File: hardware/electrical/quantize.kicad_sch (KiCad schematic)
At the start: 5 parts

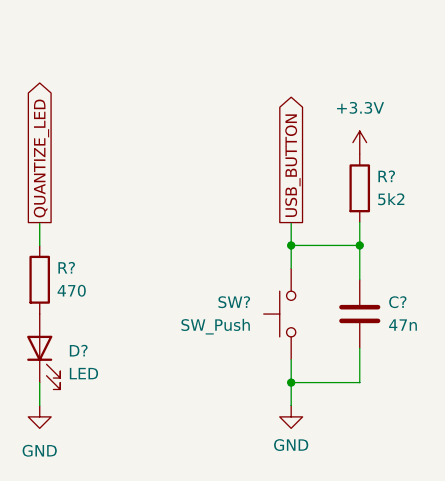
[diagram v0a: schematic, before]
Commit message: Schematic rev. 2 Add second microcontroller to handle encoder, buttons and LEDs Remove external pull-up resistors Simplify LED driver circuits Remove debouncing capacitors Rename SPI connections with standard names Use SPI1 rather than SPI2 Isolate GNDD and GLED
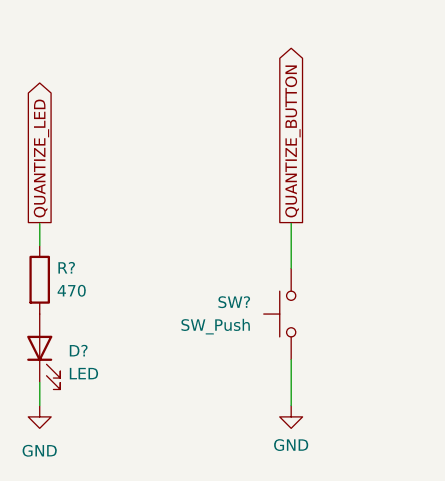
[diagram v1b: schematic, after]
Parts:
- removed C?: 47n, symbol Device:C
- removed R?: 5k2, symbol Device:R
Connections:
- net USB_BUTTON renamed QUANTIZE_BUTTON
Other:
- company: (none) -> © ANDREI ANATSKA, FRANK PLOWMAN 2022
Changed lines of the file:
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@@
 (kicad_sch (version 20211123) (generator eeschema)
   (paper "A4")
-  (junction (at 157.48 113.665) (diameter 0) (color 0 0 0 0)
+  (title_block
+    (date "2022-09-08")
+    (rev "2")
+    (company "© ANDREI ANATSKA, FRANK PLOWMAN 2022")
   )
-  (junction (at 165.1 98.425) (diameter 0) (color 0 0 0 0)
-  )
-  (junction (at 157.48 98.425) (diameter 0) (color 0 0 0 0)
-  )
-  (wire (pts (xy 165.1 102.235) (xy 165.1 98.425))
-    (stroke (width 0) (type default) (color 0 0 0 0))
-  )
-  (wire (pts (xy 157.48 113.665) (xy 165.1 113.665))
-    (stroke (width 0) (type default) (color 0 0 0 0))
-  )
-  (wire (pts (xy 157.48 98.425) (xy 165.1 98.425))
-    (stroke (width 0) (type default) (color 0 0 0 0))
-  )
-  (wire (pts (xy 165.1 113.665) (xy 165.1 109.855))
-    (stroke (width 0) (type default) (color 0 0 0 0))
-  )
-  (wire (pts (xy 165.1 95.885) (xy 165.1 98.425))
-    (stroke (width 0) (type default) (color 0 0 0 0))
-  )
-  (wire (pts (xy 157.48 95.885) (xy 157.48 98.425))
-    (stroke (width 0) (type default) (color 0 0 0 0))
-  )
-  (wire (pts (xy 157.48 113.665) (xy 157.48 116.205))
-    (stroke (width 0) (type default) (color 0 0 0 0))
-  )
-  (wire (pts (xy 157.48 98.425) (xy 157.48 100.965))
+  (wire (pts (xy 157.48 95.885) (xy 157.48 100.965))
     (stroke (width 0) (type default) (color 0 0 0 0))
   )
@@
     (stroke (width 0) (type default) (color 0 0 0 0))
   )
-  (wire (pts (xy 157.48 111.125) (xy 157.48 113.665))
+  (wire (pts (xy 157.48 111.125) (xy 157.48 116.205))
     (stroke (width 0) (type default) (color 0 0 0 0))
   )
-  (global_label "USB_BUTTON" (shape output) (at 157.48 95.885 90) (fields_autoplaced)
+  (global_label "QUANTIZE_BUTTON" (shape output) (at 157.48 95.885 90) (fields_autoplaced)
     (effects (font (size 1.27 1.27)) (justify left))
-    (property "Intersheet References" "${INTERSHEET_REFS}" (id 0) (at 157.4006 81.4976 90)
+    (property "Intersheet References" "${INTERSHEET_REFS}" (id 0) (at 157.4006 76.2967 90)
       (effects (font (size 1.27 1.27)) (justify left) hide)
     )
@@
     (pin "2")
   )
-  (symbol (lib_id "power:+3.3V") (at 165.1 88.265 0) (unit 1)
-    (in_bom yes) (on_board yes) (fields_autoplaced)
-    (property "Reference" "#PWR?" (id 0) (at 165.1 92.075 0)
-      (effects (font (size 1.27 1.27)) hide)
-    )
-    (property "Value" "+3.3V" (id 1) (at 165.1 83.185 0))
-    (property "Footprint" "" (id 2) (at 165.1 88.265 0)
-      (effects (font (size 1.27 1.27)) hide)
-    )
-    (property "Datasheet" "" (id 3) (at 165.1 88.265 0)
-      (effects (font (size 1.27 1.27)) hide)
-    )
-    (pin "1")
-  )
   (symbol (lib_id "power:GND") (at 157.48 116.205 0) (unit 1)
     (in_bom yes) (on_board yes) (fields_autoplaced)
-    (property "Reference" "#PWR?" (id 0) (at 157.48 122.555 0)
+    (property "Reference" "#PWR0156" (id 0) (at 157.48 122.555 0)
       (effects (font (size 1.27 1.27)) hide)
     )
@@
     (pin "1")
   )
-  (symbol (lib_id "Device:C") (at 165.1 106.045 0) (unit 1)
+  (symbol (lib_id "power:GND") (at 129.54 116.205 0) (unit 1)
     (in_bom yes) (on_board yes) (fields_autoplaced)
-    (property "Reference" "C?" (id 0) (at 168.275 104.7749 0)
-      (effects (font (size 1.27 1.27)) (justify left))
-    )
-    (property "Value" "47n" (id 1) (at 168.275 107.3149 0)
-      (effects (font (size 1.27 1.27)) (justify left))
-    )
-    (property "Footprint" "" (id 2) (at 166.0652 109.855 0)
+    (property "Reference" "#PWR0157" (id 0) (at 129.54 122.555 0)
       (effects (font (size 1.27 1.27)) hide)
     )
-    (property "Datasheet" "~" (id 3) (at 165.1 106.045 0)
-      (effects (font (size 1.27 1.27)) hide)
-    )
-    (pin "1")
-    (pin "2")
-  )
-  (symbol (lib_id "Device:R") (at 165.1 92.075 0) (unit 1)
-    (in_bom yes) (on_board yes) (fields_autoplaced)
-    (property "Reference" "R?" (id 0) (at 167.005 90.8049 0)
-      (effects (font (size 1.27 1.27)) (justify left))
-    )
-    (property "Value" "5k2" (id 1) (at 167.005 93.3449 0)
-      (effects (font (size 1.27 1.27)) (justify left))
-    )
-    (property "Footprint" "" (id 2) (at 163.322 92.075 90)
-      (effects (font (size 1.27 1.27)) hide)
-    )
-    (property "Datasheet" "~" (id 3) (at 165.1 92.075 0)
-      (effects (font (size 1.27 1.27)) hide)
-    )
-    (pin "1")
-    (pin "2")
-  )
-  (symbol (lib_id "power:GND") (at 129.54 116.205 0) (unit 1)
-    (in_bom yes) (on_board yes) (fields_autoplaced)
-    (property "Reference" "#PWR?" (id 0) (at 129.54 122.555 0)
-      (effects (font (size 1.27 1.27)) hide)
-    )
